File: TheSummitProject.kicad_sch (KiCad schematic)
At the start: 27 parts, among them IC1 STM32U5F7VJT6, J1 Cortex SWD, J2 USB C, SW1 SW_SPDT, Y1 16Mhz, Y2 32.768Khz

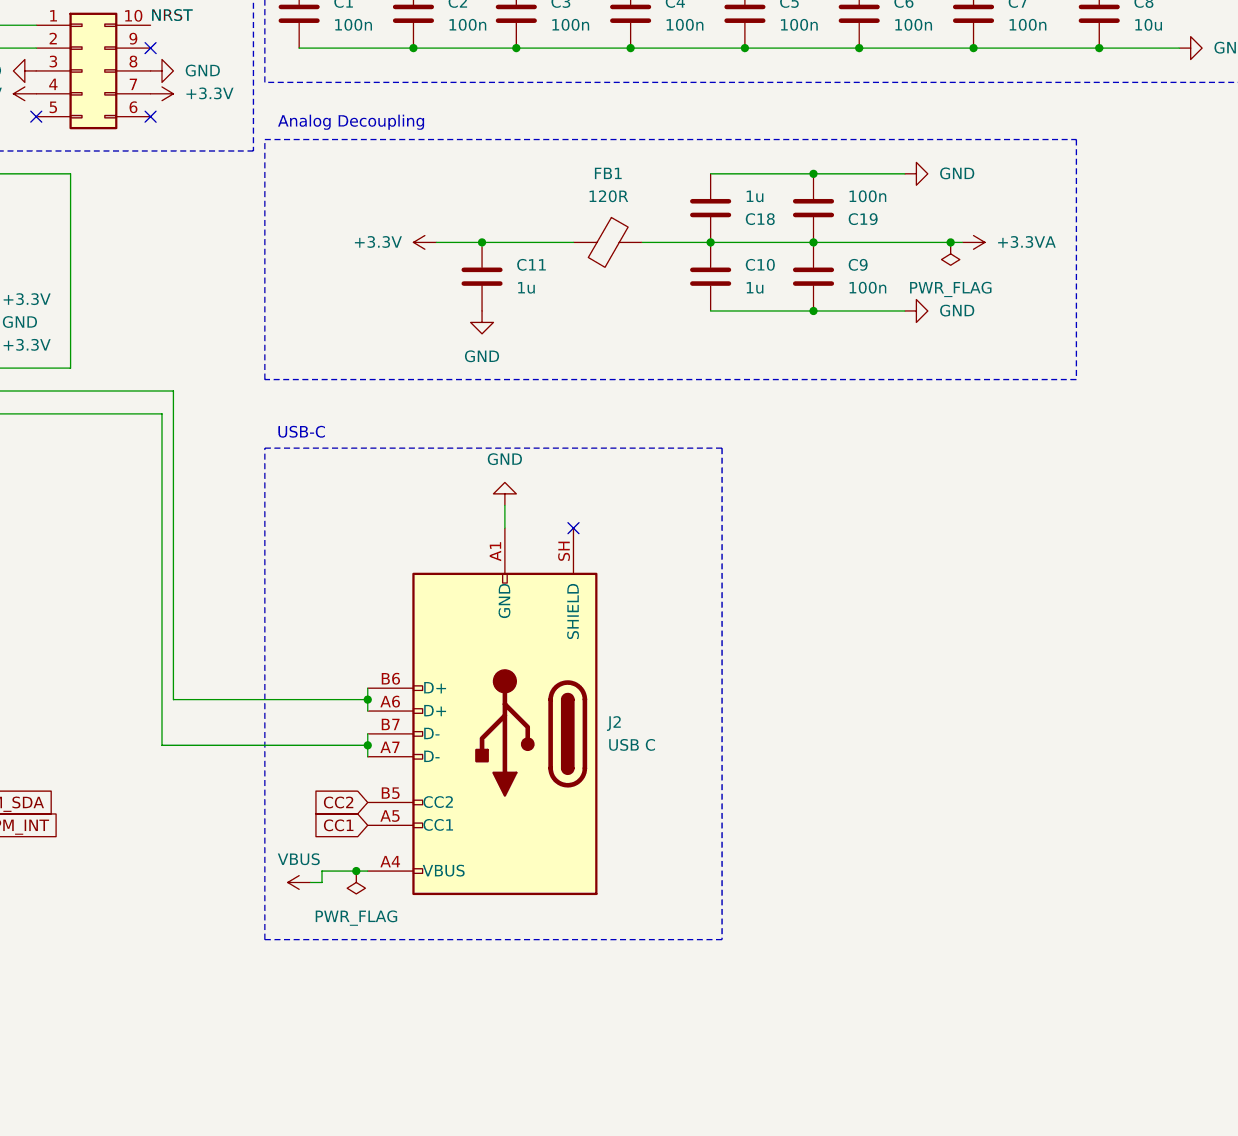
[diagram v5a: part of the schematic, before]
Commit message: added symbol library
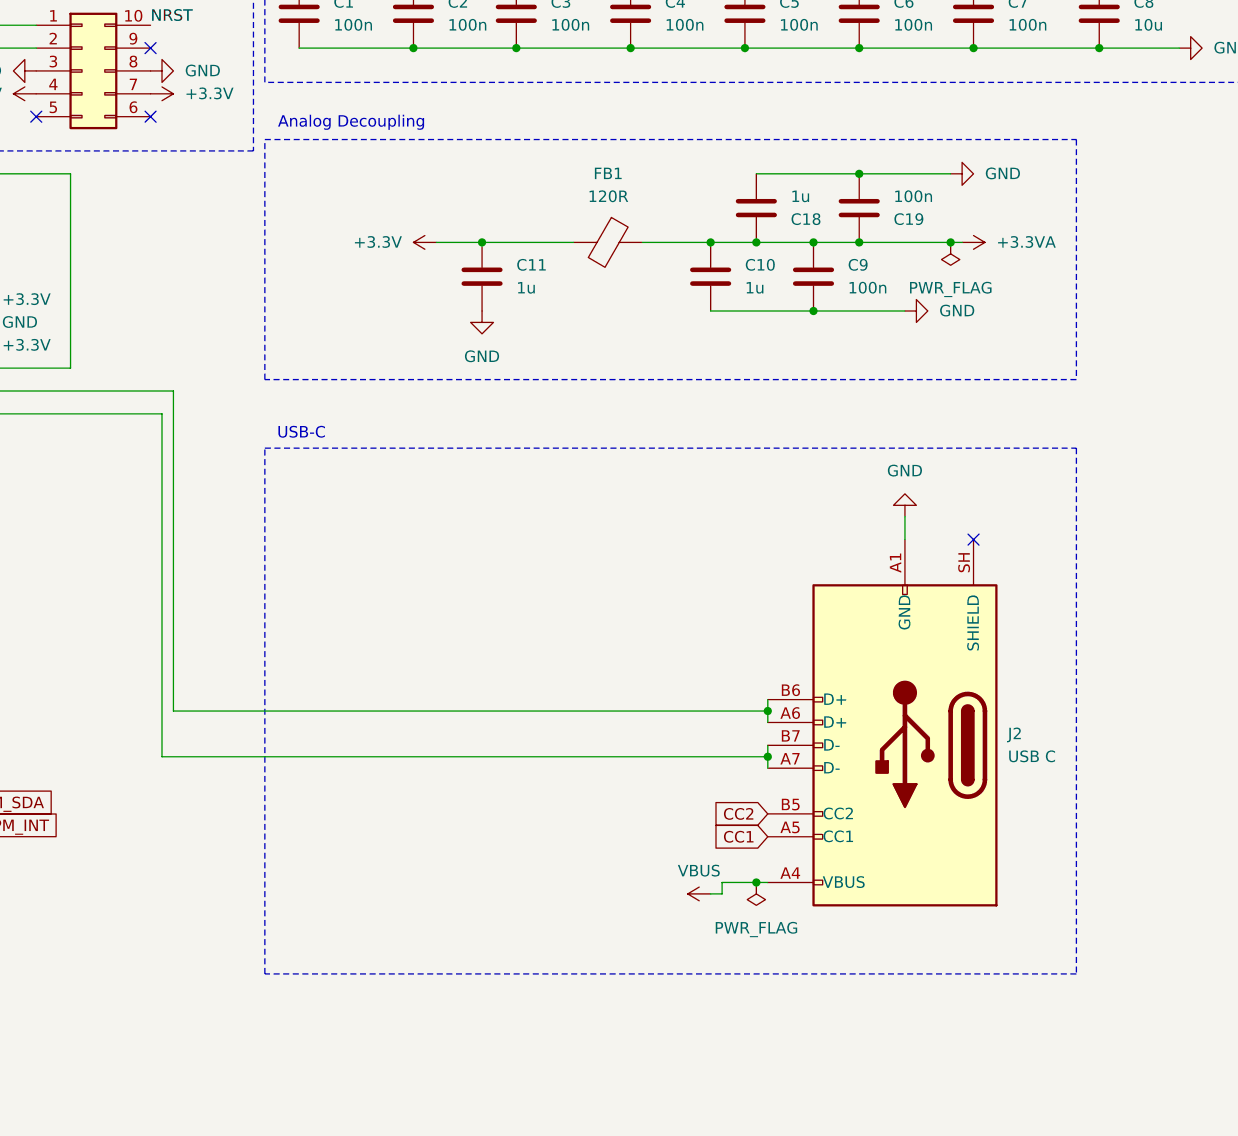
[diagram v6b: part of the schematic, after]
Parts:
- IC1: symbol STM32U5F7VJT6:STM32U5F7VJT6 -> TheSummitProject:STM32U5F7VJT6; HEIGHT (none) -> 1.6
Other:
- moved on the sheet: C18, C19, J2

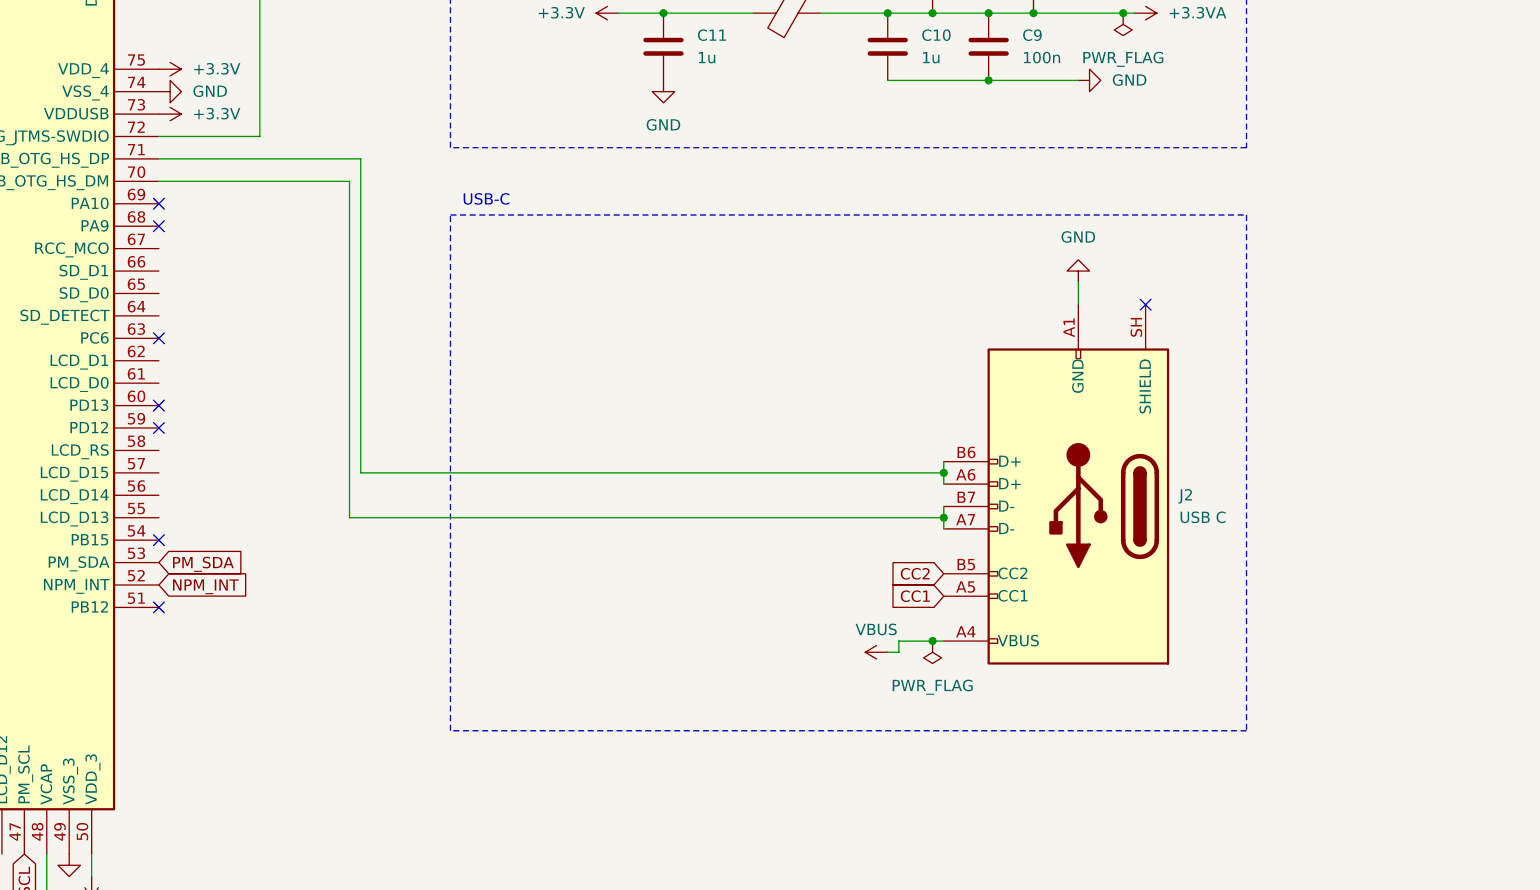
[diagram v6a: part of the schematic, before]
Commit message: added ESD protection for USB
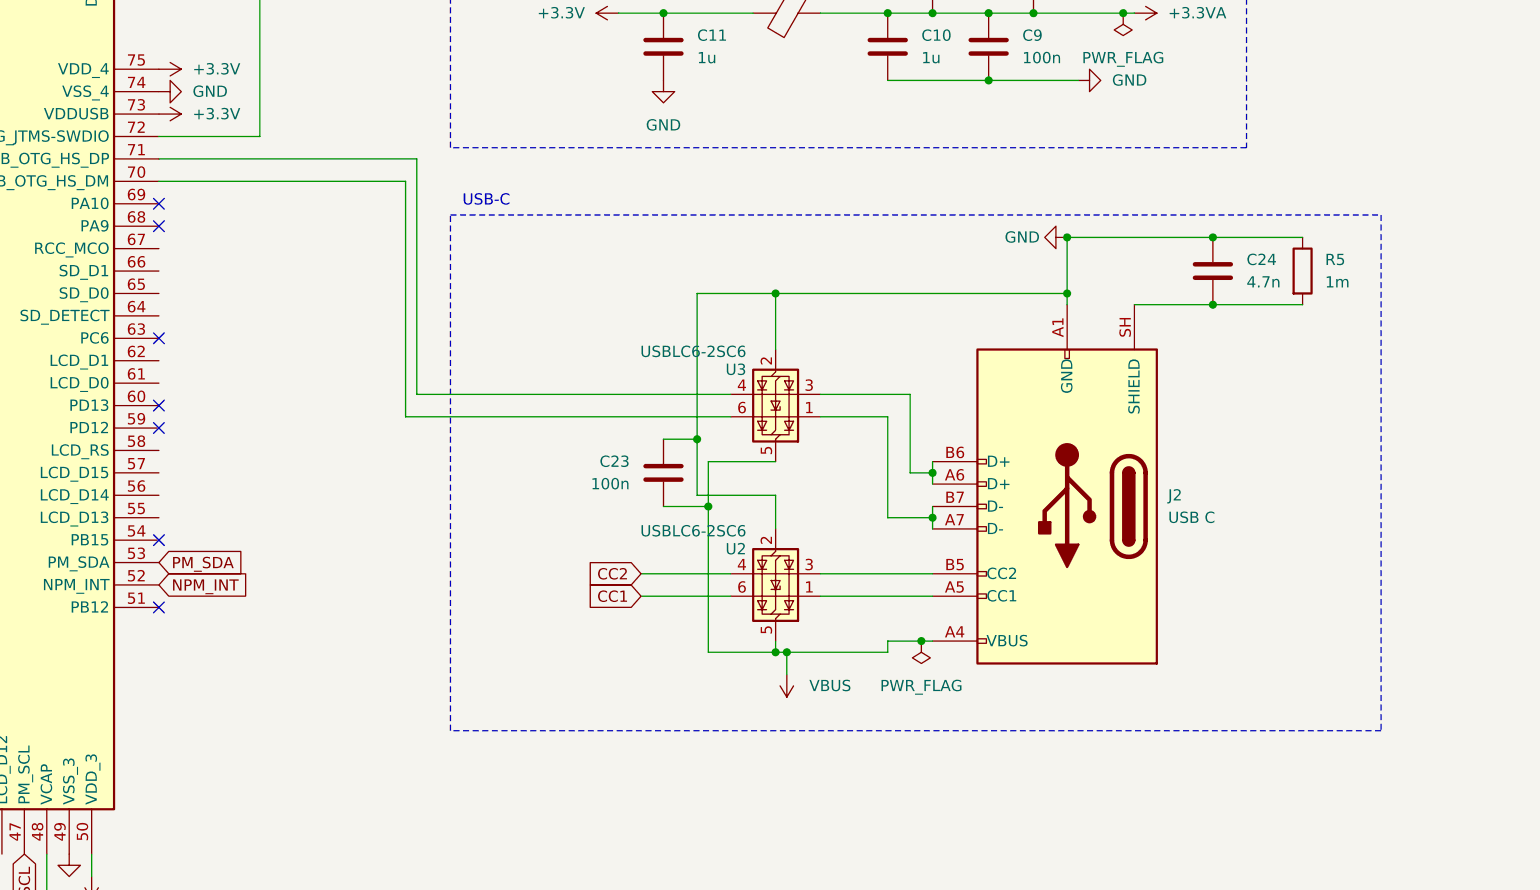
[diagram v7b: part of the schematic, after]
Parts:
- added C23: 100n, symbol Device:C
- added C24: 4.7n, symbol Device:C
- added R5: 1m, symbol Device:R
- added U2, U3: USBLC6-2SC6, Package_TO_SOT_SMD:SOT-23-6, symbol Power_Protection:USBLC6-2SC6
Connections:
- net CC1: now also U2.6 (I/O1); no longer J2.A5 (CC1)
- net CC2: now also U2.4 (I/O2); no longer J2.B5 (CC2)
- net GND: now also C23.2, C24.2, R5.1, U2.2 (GND), U3.2 (GND)
- net VBUS: now also C23.1, U2.5 (VBUS), U3.5 (VBUS)
- net at J2.A7 (D-), J2.B7 (D-): now also U3.1 (I/O1); no longer IC1.70 (USB_OTG_HS_DM)
- net at J2.A6 (D+), J2.B6 (D+): now also U3.3 (I/O2); no longer IC1.71 (USB_OTG_HS_DP)
- net at J2.SH (SHIELD): now also C24.1, R5.2
- new net: IC1.71 (USB_OTG_HS_DP), U3.4 (I/O2)
- new net: IC1.70 (USB_OTG_HS_DM), U3.6 (I/O1)
- new net: J2.A5 (CC1), U2.1 (I/O1)
- new net: J2.B5 (CC2), U2.3 (I/O2)
- no-connect marks 28 -> 27
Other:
- moved on the sheet: J2
